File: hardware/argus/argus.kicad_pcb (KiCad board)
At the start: 2 copper layers, 10 parts, among them J1 Conn_01x02, J2 Conn_01x02, J3 Conn_01x01, SW1 SW_SPST, U1 CH32V003FxPx, X1 24MHZ

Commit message: hardware: First layout proposition
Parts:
- added J3: Conn_01x01, Connector_Pin:Pin_D0.7mm_L6.5mm_W1.8mm_FlatFork, F.Cu at (167.6, 77.7)
- added J4: Conn_01x01, Connector_Pin:Pin_D0.7mm_L6.5mm_W1.8mm_FlatFork, F.Cu at (167.6, 74.9)
- J1, J2: value Conn_01x02 -> Conn_01x01; footprint Connector_Wire:SolderWire-0.5sqmm_1x02_P4.6mm_D0.9mm_OD2.1mm -> Connector_Pin:Pin_D0.7mm_L6.5mm_W1.8mm_FlatFork
- J5: renamed from J3; footprint Connector_Pin:Pin_D1.0mm_L10.0mm -> Connector_Pin:Pin_D0.7mm_L6.5mm_W1.8mm_FlatFork
- SW1: footprint Button_Switch_SMD:SW_DIP_SPSTx01_Slide_6.7x4.1mm_W6.73mm_P2.54mm_LowProfile_JPin -> Button_Switch_SMD:SW_SPST_EVQPE1; moved to B.Cu
- moved J2 21.5 mm to (150.6, 77.5), turned to 0 degrees
- moved J1 10.0 mm to (150.6, 72.6), turned to 0 degrees
- moved SW1 8.95 mm to (155.6, 75.2), turned to 90 degrees
- moved C3 3.21 mm to (154.3, 78.0)
- moved C2 2.86 mm to (154.3, 71.9)
- moved X1 2.66 mm to (154.0, 75.0)
- moved C1 2.51 mm to (156.8, 76.3)
- moved J5 2.26 mm to (167.6, 72.1)
- moved U1 1.81 mm to (161.9, 74.9)
- moved C4 1.70 mm to (156.8, 73.2)
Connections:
- J2 pad 1: /D+ -> GND
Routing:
- added copper zone on F.Cu, net GND
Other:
- board outline added: 20.6 x 8.9 mm

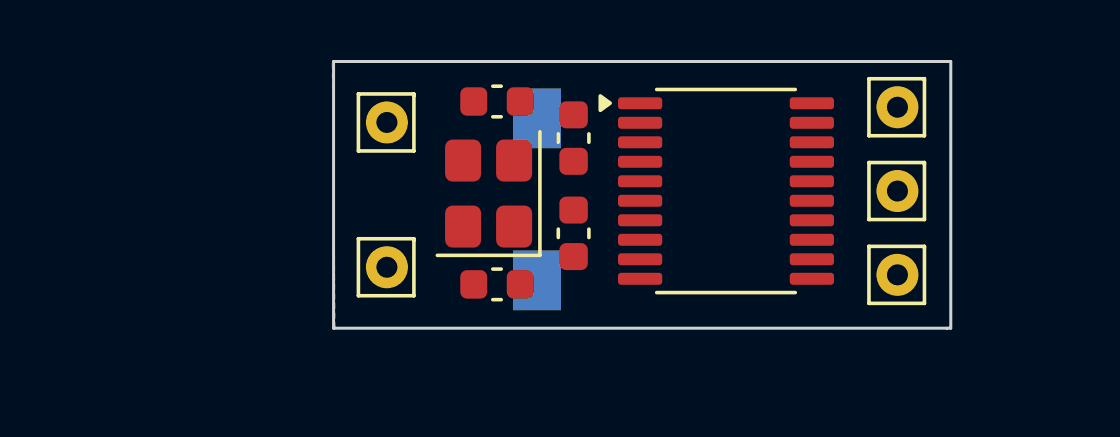
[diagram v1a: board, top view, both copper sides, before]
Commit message: hardware: Changes XTAL footprint. Adjusts layout
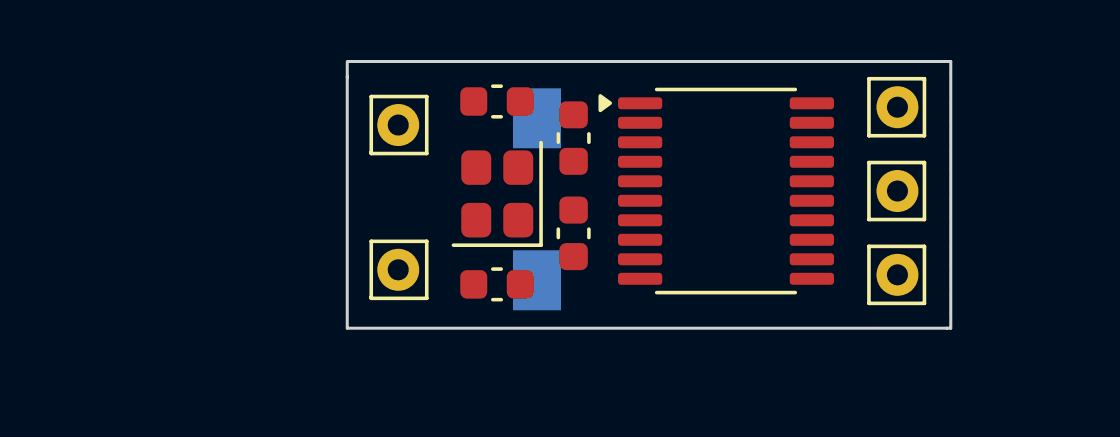
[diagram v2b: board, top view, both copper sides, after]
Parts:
- X1: footprint Crystal:Crystal_SMD_Abracon_ABM8G-4Pin_3.2x2.5mm -> Crystal:Crystal_SMD_2520-4Pin_2.5x2.0mm
- moved J1 4.93 mm to (151.0, 77.6), turned to 180 degrees
- moved J2 4.76 mm to (151.0, 72.7), turned to 180 degrees
- moved X1 0.29 mm to (154.3, 75.0)
- turned C3 to 180 degrees
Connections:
- X1 pad 2: Net-(U1-PA1) -> GND
- X1 pad 3: (no net) -> Net-(U1-PA1)
- X1 pad 4: (no net) -> GND
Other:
- board size 20.6 x 8.9 mm -> 20.1 x 8.9 mm

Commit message: hardware: Connects layout elements #1
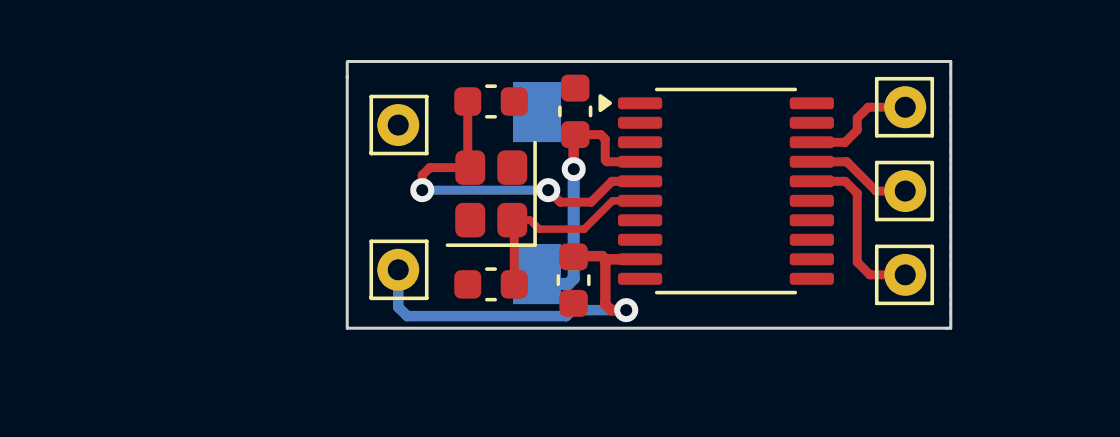
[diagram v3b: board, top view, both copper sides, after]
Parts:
- moved C1 1.56 mm to (156.8, 77.9), turned to -90 degrees
- moved C4 0.89 mm to (156.9, 72.3)
- moved J3 0.26 mm to (167.9, 77.7)
- moved J4 0.26 mm to (167.9, 74.9)
- moved J5 0.26 mm to (167.9, 72.1)
- moved SW1 0.20 mm to (155.6, 75.0)
- moved X1 0.20 mm to (154.1, 75.0)
- moved C2 0.20 mm to (154.1, 71.9)
- moved C3 0.20 mm to (154.1, 78.0)
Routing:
- net +5V: track 0.00 -> 13.6 mm, vias 0 -> 1
- net Net-(U1-PA1): track 0.00 -> 12.2 mm, vias 0 -> 2
- net /NRST: track 0.00 -> 9.37 mm, vias 0 -> 1
- net Net-(U1-PA2): track 0.00 -> 6.75 mm
- net /D+: track 0.00 -> 5.75 mm
- net /SWIO: track 0.00 -> 3.83 mm
- net /D-: track 0.00 -> 3.52 mm
- added copper zone on B.Cu, net GND

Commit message: hardware: Connects layout elements #2
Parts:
- moved SW1 1.28 mm to (156.9, 75.1), turned to 0 degrees
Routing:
- net +5V: track 13.6 -> 8.42 mm
- net Net-(U1-PA1): track 12.2 -> 13.2 mm
- net /NRST: track 9.37 -> 8.67 mm
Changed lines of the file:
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@@
 	(footprint "Button_Switch_SMD:SW_SPST_EVQPE1"
 		(layer "B.Cu")
-		(at 155.625 75 90)
+		(at 156.9 75.1)
 		(descr "Light Touch Switch, https://industrial.panasonic.com/cdbs/www-data/pdf/ATK0000/ATK0000CE7.pdf")
 		(property "Reference" "SW1"
-			(at 0 2.65 90)
+			(at 0 2.65 0)
 			(layer "B.SilkS")
 			(hide yes)
@@
 		)
 		(property "Value" "SW_SPST"
-			(at 0 -3 90)
+			(at 0 -3 0)
 			(layer "B.Fab")
 			(hide yes)
@@
 		)
 		(property "Datasheet" ""
-			(at 0 0 270)
+			(at 0 0 180)
 			(unlocked yes)
 			(layer "B.Fab")
@@
 		)
 		(property "Description" "Single Pole Single Throw (SPST) switch"
-			(at 0 0 270)
+			(at 0 0 180)
 			(unlocked yes)
 			(layer "B.Fab")
@@
 		(duplicate_pad_numbers_are_jumpers no)
 		(fp_line
+			(start -3.1 -1.85)
+			(end 3.1 -1.85)
+			(stroke
+				(width 0.12)
+				(type solid)
+			)
+			(layer "B.SilkS")
+		)
+		(fp_line
+			(start -3.1 -1.2)
+			(end -3.1 -1.85)
+			(stroke
+				(width 0.12)
+				(type solid)
+			)
+			(layer "B.SilkS")
+		)
+		(fp_line
+			(start -3.1 1.85)
+			(end -3.1 1.2)
+			(stroke
+				(width 0.12)
+				(type solid)
+			)
+			(layer "B.SilkS")
+		)
+		(fp_line
 			(start 3.1 -1.85)
 			(end 3.1 -1.2)
@@
 		)
 		(fp_line
-			(start -3.1 -1.85)
-			(end 3.1 -1.85)
-			(stroke
-				(width 0.12)
-				(type solid)
-			)
-			(layer "B.SilkS")
-		)
-		(fp_line
-			(start -3.1 -1.2)
-			(end -3.1 -1.85)
+			(start 3.1 1.85)
+			(end -3.1 1.85)
 			(stroke
 				(width 0.12)
@@
 		)
 		(fp_line
-			(start 3.1 1.85)
-			(end -3.1 1.85)
-			(stroke
-				(width 0.12)
-				(type solid)
-			)
-			(layer "B.SilkS")
-		)
-		(fp_line
-			(start -3.1 1.85)
-			(end -3.1 1.2)
-			(stroke
-				(width 0.12)
-				(type solid)
-			)
-			(layer "B.SilkS")
+			(start -3.95 -2)
+			(end -3.95 2)
+			(stroke
+				(width 0.05)
+				(type solid)
+			)
+			(layer "B.CrtYd")
+		)
+		(fp_line
+			(start -3.95 2)
+			(end 3.95 2)
+			(stroke
+				(width 0.05)
+				(type solid)
+			)
+			(layer "B.CrtYd")
 		)
 		(fp_line
@@
 		)
 		(fp_line
-			(start -3.95 -2)
-			(end -3.95 2)
-			(stroke
-				(width 0.05)
-				(type solid)
-			)
-			(layer "B.CrtYd")
-		)
-		(fp_line
 			(start 3.95 2)
 			(end 3.95 -2)
@@
 		)
 		(fp_line
-			(start -3.95 2)
-			(end 3.95 2)
-			(stroke
-				(width 0.05)
-				(type solid)
-			)
-			(layer "B.CrtYd")
+			(start -3 -1.75)
+			(end -3 1.75)
+			(stroke
+				(width 0.1)
+				(type solid)
+			)
+			(layer "B.Fab")
+		)
+		(fp_line
+			(start -3 1.75)
+			(end 3 1.75)
+			(stroke
+				(width 0.1)
+				(type solid)
+			)
+			(layer "B.Fab")
+		)
+		(fp_line
+			(start -1.4 -0.7)
+			(end -1.4 0.7)
+			(stroke
+				(width 0.1)
+				(type solid)
+			)
+			(layer "B.Fab")
+		)
+		(fp_line
+			(start -1.4 0.7)
+			(end 1.4 0.7)
+			(stroke
+				(width 0.1)
+				(type solid)
+			)
+			(layer "B.Fab")
+		)
+		(fp_line
+			(start 1.4 -0.7)
+			(end -1.4 -0.7)
+			(stroke
+				(width 0.1)
+				(type solid)
+			)
+			(layer "B.Fab")
+		)
+		(fp_line
+			(start 1.4 0.7)
+			(end 1.4 -0.7)
+			(stroke
+				(width 0.1)
+				(type solid)
+			)
+			(layer "B.Fab")
 		)
 		(fp_line
@@
 		)
 		(fp_line
-			(start -3 -1.75)
-			(end -3 1.75)
-			(stroke
-				(width 0.1)
-				(type solid)
-			)
-			(layer "B.Fab")
-		)
-		(fp_line
-			(start 1.4 -0.7)
-			(end -1.4 -0.7)
-			(stroke
-				(width 0.1)
-				(type solid)
-			)
-			(layer "B.Fab")
-		)
-		(fp_line
-			(start -1.4 -0.7)
-			(end -1.4 0.7)
-			(stroke
-				(width 0.1)
-				(type solid)
-			)
-			(layer "B.Fab")
-		)
-		(fp_line
-			(start 1.4 0.7)
-			(end 1.4 -0.7)
-			(stroke
-				(width 0.1)
-				(type solid)
-			)
-			(layer "B.Fab")
-		)
-		(fp_line
-			(start -1.4 0.7)
-			(end 1.4 0.7)
-			(stroke
-				(width 0.1)
-				(type solid)
-			)
-			(layer "B.Fab")
-		)
-		(fp_line
 			(start 3 1.75)
 			(end 3 -1.75)
@@
 			(layer "B.Fab")
 		)
-		(fp_line
-			(start -3 1.75)
-			(end 3 1.75)
-			(stroke
-				(width 0.1)
-				(type solid)
-			)
-			(layer "B.Fab")
-		)
 		(pad "1" smd rect
-			(at -2.7 0 90)
+			(at -2.7 0)
 			(size 2 1.6)
 			(layers "B.Cu" "B.Mask" "B.Paste")
@@
 		)
 		(pad "2" smd rect
-			(at 2.7 0 90)
+			(at 2.7 0)
 			(size 2 1.6)
 			(layers "B.Cu" "B.Mask" "B.Paste")
@@
 	)
 	(segment
-		(start 156.85 77.85)
-		(end 156.675 78.025)
-		(width 0.4)
-		(layer "B.Cu")
-		(net "/NRST")
-	)
-	(segment
-		(start 156.675 78.025)
-		(end 155.745 78.025)
-		(width 0.4)
+		(start 154.2 75.1)
+		(end 154.75 75.65)
+		(width 0.3)
+		(layer "B.Cu")
+		(net "/NRST")
+	)
+	(segment
+		(start 154.75 75.65)
+		(end 156.8 75.65)
+		(width 0.3)
+		(layer "B.Cu")
+		(net "/NRST")
+	)
+	(segment
+		(start 156.8 75.65)
+		(end 156.85 75.6)
+		(width 0.3)
 		(layer "B.Cu")
 		(net "/NRST")
@@
 	(segment
 		(start 156.85 74.2)
-		(end 156.85 77.85)
-		(width 0.4)
-		(layer "B.Cu")
-		(net "/NRST")
-	)
-	(segment
-		(start 155.745 78.025)
-		(end 155.625 77.905)
+		(end 156.85 75.6)
 		(width 0.4)
 		(layer "B.Cu")
@@
 	)
 	(segment
+		(start 155.3 73.9)
+		(end 152.8 73.9)
+		(width 0.3)
+		(layer "B.Cu")
+		(net "Net-(U1-PA1)")
+	)
+	(segment
 		(start 156 74.9)
+		(end 155.55 74.45)
+		(width 0.3)
+		(layer "B.Cu")
+		(net "Net-(U1-PA1)")
+	)
+	(segment
+		(start 152.8 73.9)
 		(end 151.8 74.9)
+		(width 0.3)
+		(layer "B.Cu")
+		(net "Net-(U1-PA1)")
+	)
+	(segment
+		(start 155.55 74.15)
+		(end 155.3 73.9)
+		(width 0.3)
+		(layer "B.Cu")
+		(net "Net-(U1-PA1)")
+	)
+	(segment
+		(start 155.55 74.45)
+		(end 155.55 74.15)
 		(width 0.3)
 		(layer "B.Cu")
@@
 	)
 	(segment
-		(start 156.87 77.1)
-		(end 156.845 77.125)
-		(width 0.35)
+		(start 156.845 77.125)
+		(end 155.810207 77.125)
+		(width 0.3)
 		(layer "F.Cu")
 		(net "+5V")
@@
 	)
 	(segment
-		(start 157.905 78.695)
-		(end 157.9 78.7)
-		(width 0.35)
-		(layer "F.Cu")
-		(net "+5V")
-	)
-	(segment
-		(start 158.1 78.9)
-		(end 158.6 78.9)
-		(width 0.35)
+		(start 155.810207 77.125)
+		(end 155.70378 77.231427)
+		(width 0.3)
 		(layer "F.Cu")
 		(net "+5V")
@@
 	)
 	(segment
-		(start 157.905 77.205)
-		(end 157.905 78.695)
-		(width 0.35)
-		(layer "F.Cu")
-		(net "+5V")
-	)
-	(segment
 		(start 157.8 77.1)
 		(end 156.87 77.1)
@@
 		(net "+5V")
 	)
-	(segment
-		(start 157.9 78.7)
-		(end 158.1 78.9)
-		(width 0.35)
-		(layer "F.Cu")
-		(net "+5V")
-	)
 	(via
-		(at 158.6 78.9)
+		(at 155.70378 77.231427)
 		(size 0.8)
 		(drill 0.4)
@@
 	)
 	(segment
-		(start 151.3 79.1)
-		(end 151 78.8)
-		(width 0.35)
-		(layer "B.Cu")
-		(net "+5V")
-	)
-	(segment
-		(start 151 78.8)
+		(start 155.6 77.335207)
+		(end 155.70378 77.231427)
+		(width 0.35)
+		(layer "B.Cu")
+		(net "+5V")
+	)
+	(segment
+		(start 155.6 77.3)
+		(end 155.6 77.412)
+		(width 0.35)
+		(layer "B.Cu")
+		(net "+5V")
+	)
+	(segment
+		(start 155.456 77.556)
 		(end 151 77.556)
 		(width 0.35)
@@
 	)
 	(segment
-		(start 158.6 78.9)
-		(end 156.8 78.9)
-		(width 0.35)
-		(layer "B.Cu")
-		(net "+5V")
-	)
-	(segment
-		(start 156.6 79.1)
-		(end 151.3 79.1)
-		(width 0.35)
-		(layer "B.Cu")
-		(net "+5V")
-	)
-	(segment
-		(start 156.8 78.9)
-		(end 156.6 79.1)
-		(width 0.35)
-		(layer "B.Cu")
+		(start 155.6 77.412)
+		(end 155.456 77.556)
+		(width 0.35)
+		(layer "B.Cu")
+		(net "+5V")
+	)
+	(segment
+		(start 155.6 77.412)
+		(end 155.6 77.335207)
+		(width 0.35)
+		(layer "B.Cu")

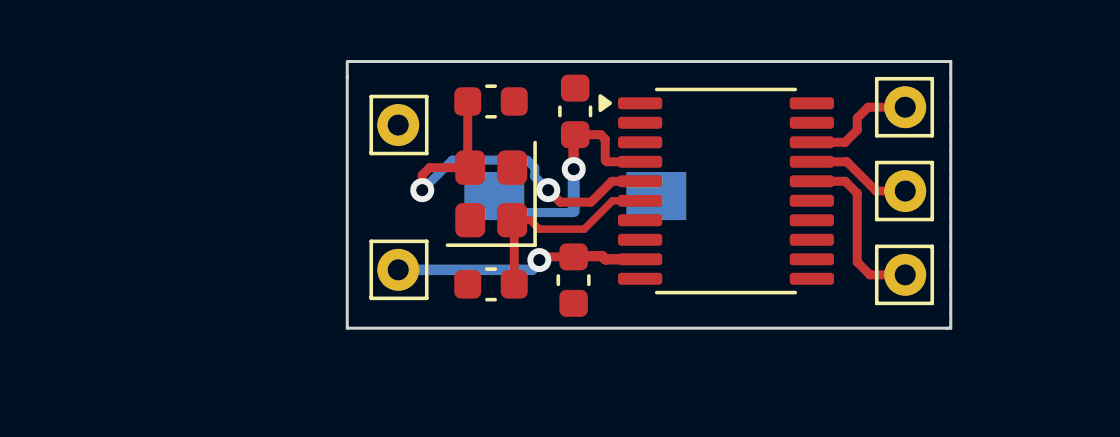
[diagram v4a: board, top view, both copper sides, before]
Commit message: hardware: Connects layout elements #3
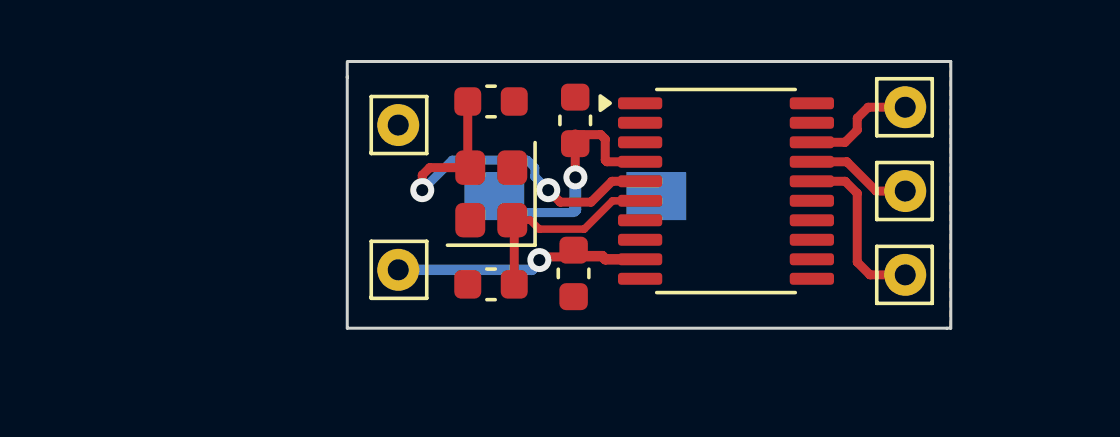
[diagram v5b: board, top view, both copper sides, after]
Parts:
- moved C4 0.30 mm to (156.9, 72.6)
- moved C1 0.23 mm to (156.8, 77.7)
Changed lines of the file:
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@@
 	(footprint "Capacitor_SMD:C_0603_1608Metric"
 		(layer "F.Cu")
-		(at 156.9 72.275 90)
+		(at 156.9 72.575 90)
 		(descr "Capacitor SMD 0603 (1608 Metric), square (rectangular) end terminal, IPC-7351 nominal, (Body size source: IPC-SM-782 page 76, https://www.pcb-3d.com/wordpress/wp-content/uploads/ipc-sm-782a_amendment_1_and_2.pdf)")
 		(tags "capacitor")
@@
 	(footprint "Capacitor_SMD:C_0603_1608Metric"
 		(layer "F.Cu")
-		(at 156.845 77.9 -90)
+		(at 156.845 77.675 -90)
 		(descr "Capacitor SMD 0603 (1608 Metric), square (rectangular) end terminal, IPC-7351 nominal, (Body size source: IPC-SM-782 page 76, https://www.pcb-3d.com/wordpress/wp-content/uploads/ipc-sm-782a_amendment_1_and_2.pdf)")
 		(tags "capacitor")
@@
 	)
 	(segment
-		(start 156.85 74.2)
-		(end 156.845 74.195)
+		(start 156.904821 74.474202)
+		(end 156.85 74.419381)
 		(width 0.35)
+		(layer "F.Cu")
+		(net "/NRST")
+	)
+	(segment
+		(start 156.904821 74.474202)
+		(end 156.904821 74.254821)
+		(width 0.35)
+		(layer "F.Cu")
+		(net "/NRST")
+	)
+	(segment
+		(start 156.9 73.35)
+		(end 156.9 74.469381)
+		(width 0.3)
+		(layer "F.Cu")
+		(net "/NRST")
+	)
+	(segment
+		(start 157.9 73.2)
+		(end 157.75 73.05)
+		(width 0.3)
+		(layer "F.Cu")
+		(net "/NRST")
+	)
+	(segment
+		(start 159.0625 73.955)
+		(end 157.955 73.955)
+		(width 0.3)
+		(layer "F.Cu")
+		(net "/NRST")
+	)
+	(segment
+		(start 156.9 74.469381)
+		(end 156.904821 74.474202)
+		(width 0.3)
+		(layer "F.Cu")
+		(net "/NRST")
+	)
+	(segment
+		(start 157.9 73.9)
+		(end 157.9 73.2)
+		(width 0.3)
 		(layer "F.Cu")
 		(net "/NRST")
@@
 		(net "/NRST")
 	)
-	(segment
-		(start 156.845 74.195)
-		(end 156.845 73.105)
-		(width 0.35)
-		(layer "F.Cu")
-		(net "/NRST")
-	)
-	(segment
-		(start 157.9 73.2)
-		(end 157.75 73.05)
-		(width 0.3)
-		(layer "F.Cu")
-		(net "/NRST")
-	)
-	(segment
-		(start 159.0625 73.955)
-		(end 157.955 73.955)
-		(width 0.3)
-		(layer "F.Cu")
-		(net "/NRST")
-	)
-	(segment
-		(start 156.86 73.955)
-		(end 156.85 73.965)
-		(width 0.35)
-		(layer "F.Cu")
-		(net "/NRST")
-	)
-	(segment
-		(start 157.9 73.9)
-		(end 157.9 73.2)
-		(width 0.3)
-		(layer "F.Cu")
-		(net "/NRST")
-	)
-	(segment
-		(start 156.85 73.965)
-		(end 156.85 74.2)
-		(width 0.35)
-		(layer "F.Cu")
-		(net "/NRST")
-	)
 	(via
-		(at 156.85 74.2)
+		(at 156.904821 74.474202)
 		(size 0.8)
 		(drill 0.4)
@@
 	)
 	(segment
+		(start 156.9 75.55)
+		(end 156.85 75.6)
+		(width 0.4)
+		(layer "B.Cu")
+		(net "/NRST")
+	)
+	(segment
 		(start 154.2 75.1)
 		(end 154.75 75.65)
@@
 	)
 	(segment
+		(start 156.904821 74.474202)
+		(end 156.9 74.479023)
+		(width 0.4)
+		(layer "B.Cu")
+		(net "/NRST")
+	)
+	(segment
 		(start 154.75 75.65)
 		(end 156.8 75.65)
@@
 	)
 	(segment
-		(start 156.85 74.2)
-		(end 156.85 75.6)
+		(start 156.9 74.479023)
+		(end 156.9 75.55)
 		(width 0.4)
 		(layer "B.Cu")
@@
 	(zone
 		(net "GND")
-		(layer "F.Cu")
-		(hatch edge 0.5)
+		(layers "F.Cu" "B.Cu")
+		(hatch full 0.5)
 		(connect_pads
-			(clearance 0.5)
+			(clearance 0.25)
 		)
 		(min_thickness 0.25)
 		(fill yes
-			(thermal_gap 0.5)
-			(thermal_bridge_width 0.5)
+			(thermal_gap 0.25)
+			(thermal_bridge_width 0.25)
 			(island_removal_mode 0)
 		)
